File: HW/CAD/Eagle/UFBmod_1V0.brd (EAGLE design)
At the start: 99.7 x 100 mm, 27 parts, among them Q0921 ABS07-32.768KHZ, U0611 MR44V064BMAZAATL, U0911 BNO085, U1311 TPS62745DSSR

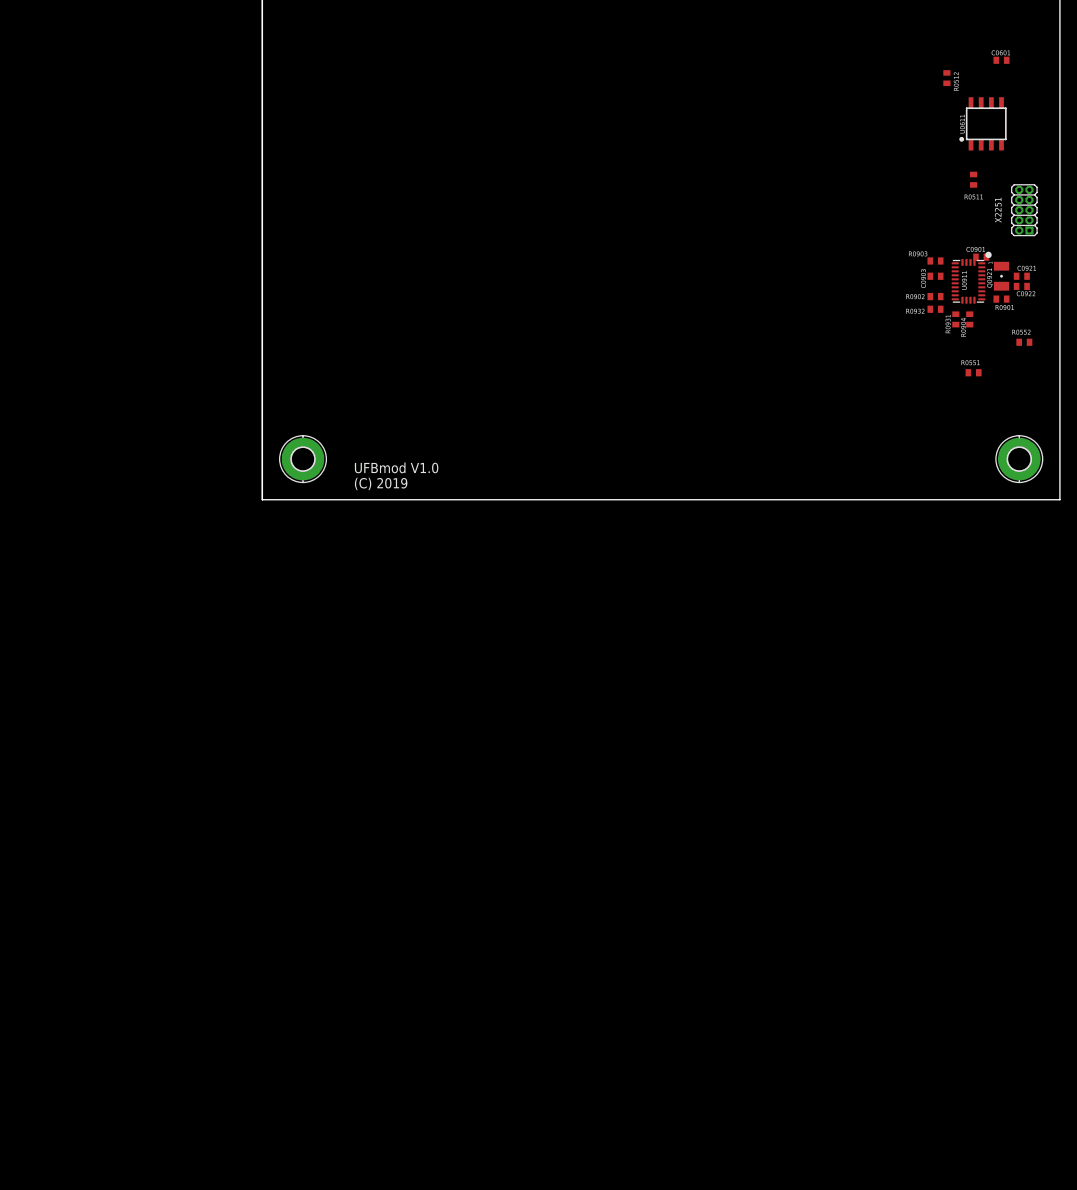
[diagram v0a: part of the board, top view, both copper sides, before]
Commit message: HW_1V0 - CAD/Eagle - Digilent Cmod A7 included, some unwanted sheets removed
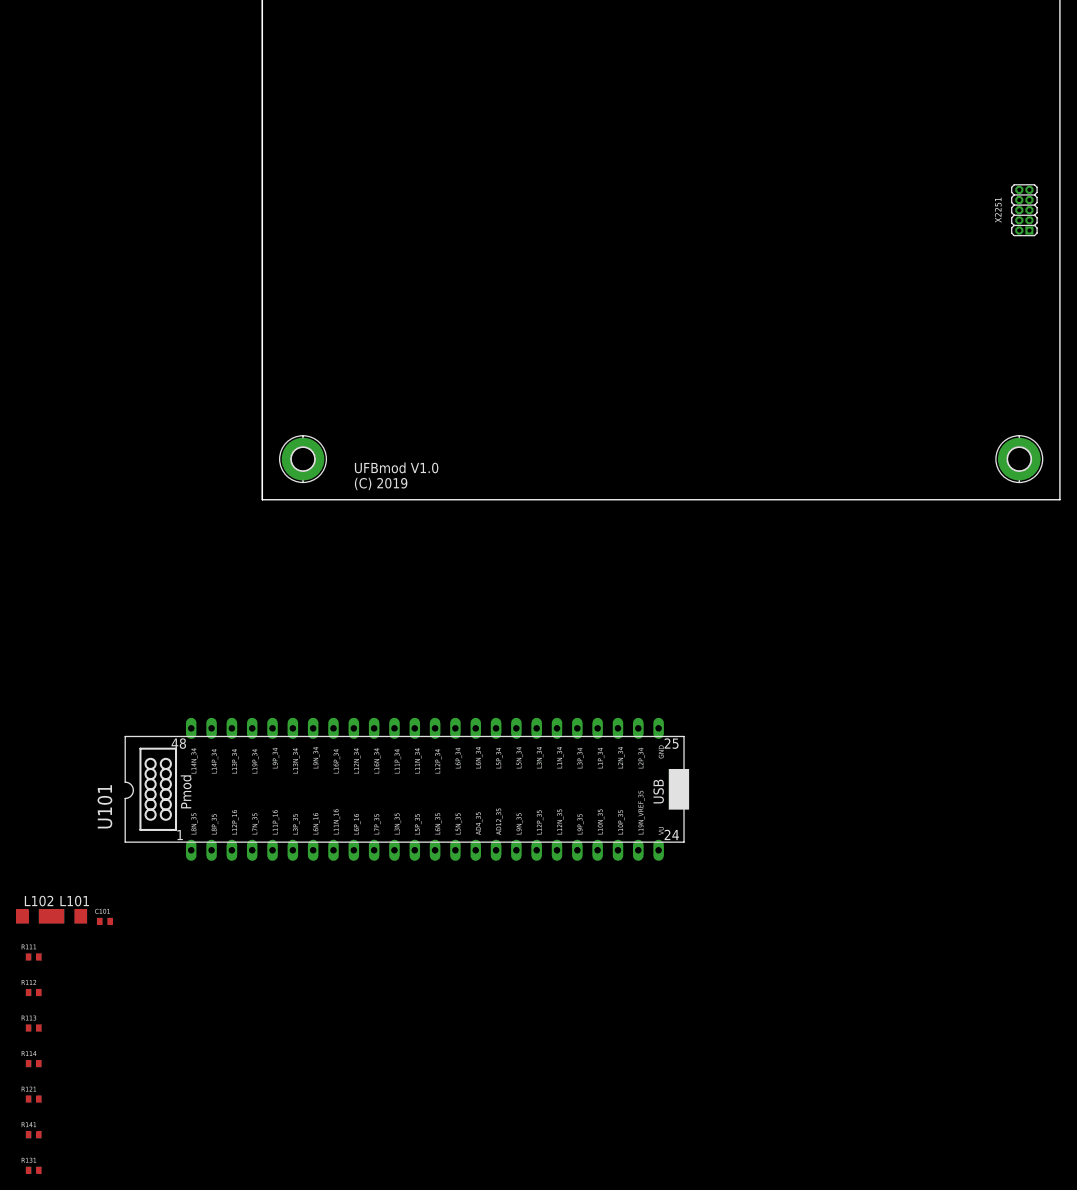
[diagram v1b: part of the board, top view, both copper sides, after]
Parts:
- removed C0601, C0901, C0903: 100nF, df4iah_rcl:C0402
- removed C0921, C0922: 22pF, df4iah_rcl:C0402
- removed Q0921: ABS07-32.768KHZ, df4iah_crystal:ABS07
- removed R0511, R0512: 1kR, df4iah_rcl:R0402
- removed R0551, R0552: 3R, df4iah_rcl:R0402
- removed R0901, R0902, R0904: 33R, df4iah_rcl:R0402
- removed R0903: 47R, df4iah_rcl:R0402
- removed R0931, R0932: 3.9kR, df4iah_rcl:R0402
- removed U0611: MR44V064BMAZAATL, df4iah_memory:SOIC8_150MIL
- removed U0911: BNO085, df4iah_sensors:BNO085_LGA28
- added C101: 100nF, df4iah_rcl:C0402
- added L101, L102: 300R, df4iah_rcl:R1206
- added R111, R112, R113, R114, R121, R131, R141: 47R, df4iah_rcl:R0402
- added U101: DIGILENT_CMOD_A7, df4iah_fpga:DIGILENT_CMOD_A7__DIP48
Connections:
- removed net BNO_CAP: C0903.1, U0911.9
- removed net BNO_CLKSEL1_XOUT32: C0922.1, Q0921.1, U0911.26
- removed net BNO_ENV_SCL: R0932.1, U0911.15
- removed net BNO_ENV_SDA: R0931.1, U0911.16
- removed net BNO_H_CSN: R0904.2, U0911.18
- removed net BNO_INTN: R0902.2, U0911.14
- removed net BNO_MISO: R0901.2, U0911.20
- removed net BNO_PS0_WAKE: R0903.2, U0911.6
- removed net BNO_XIN32: C0921.1, Q0921.2, U0911.27
- removed net PA10: R0511.1, U0611.5
- removed net PA9: R0512.1, U0611.6
- removed net PC10: R0552.1
- removed net PC12: R0551.1
- removed net SPI3_MOSI: R0551.2
- removed net SPI3_SCK: R0552.2
- new net +5V: L101.1
- new net FPGA_MISO: R114.1, U101.42
- new net FPGA_MOSI: R113.1, U101.43
- new net FPGA_SCLK: R111.1, U101.45
- new net FPGA_SELN: R112.1, U101.44
- new net FPGA_TRX_CLKO: R141.2, U101.21
- new net FPGA_TRX_IRQ: R121.1, U101.40
- new net FPGA_TRX_RESETN: R131.2, U101.20
- new net TRX_CLKO: R141.1
- new net TRX_IRQ: R121.2
- new net TRX_MISO: R114.2
- new net TRX_MOSI: R113.2
- new net TRX_RESETN: R131.1
- new net TRX_RXCLKN: U101.48
- new net TRX_RXCLKP: U101.47
- new net TRX_RXDN09N: U101.37
- new net TRX_RXDN24N: U101.1
- new net TRX_RXDP09P: U101.38
- new net TRX_RXDP24P: U101.2
- new net TRX_SCLK: R111.2
- new net TRX_SELN: R112.2
- new net TRX_TXCLKN: U101.19
- new net TRX_TXCLKP: U101.18
- new net TRX_TXDN: U101.34
- new net TRX_TXDP: U101.35
- new net VCCA: C101.2, L101.2, U101.24
- new net VSSA: C101.1, L102.2, U101.25
- net +3V3: no longer C0601.2, C0901.1, R0511.2, R0512.2, R0931.2, R0932.2, U0611.8, U0911.28, U0911.3, U0911.5
- net GND: now also L102.1; no longer C0601.1, C0901.2, C0903.2, C0921.2, C0922.2, U0611.1, U0611.2, U0611.3, U0611.4, U0611.7, U0911.10, U0911.2, U0911.25

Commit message: HW_1V0 - CAD/Eagle - schematics for the RF area expanded
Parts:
- removed R141: 47R, df4iah_rcl:R0402
- added C311, C312, C406, C407, C408, C511, C551, C552, C553: 100nF, df4iah_rcl:C0402
- added C321, C401: 1uF, df4iah_rcl:C0402
- added C403, C404, C521, C531, C532: 1nF, df4iah_rcl:C0402
- added C411, C412: 10nF, df4iah_rcl:C0402
- added C413: 56pF, df4iah_rcl:C0402
- added L401, L402, L403, L404: 300R, df4iah_rcl:R1206
- added L421: MURATA DXW21HN5011BL, df4iah_balun:DXW21HN5011BL
- added L422: Johanson 2450BL15B050E, df4iah_balun:2450BL15B050
- added L521: ? nH, df4iah_rcl:L1812
- added R211, R212: 3.9kR, df4iah_rcl:R0402
- added R321: 100kR, df4iah_rcl:R0402
- added R413: 100R, df4iah_rcl:R0402
- added U301: MAX5217, df4iah_dac:µMAX8
- added U401: AT86RF215-ZU, df4iah_rf:QFN48_7X7-0P5-PAD
- added U411: ASVTX-13-D-26.000MHZ-I05-T, df4iah_osc:ASVTX-13
- added U511: PE4259, df4iah_rf:SC-70_6-LEAD_2X1MM25_0P65
- added U521: (no value), df4iah_rf:QFN16-3X3-0P5-PAD
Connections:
- net FPGA_TRX_RESETN renamed FPGA_TRX_RSTN
- removed net TRX_RESETN: R131.1
- removed net TRX_RXDN09N: U101.37
- removed net TRX_RXDN24N: U101.1
- removed net TRX_RXDP09P: U101.38
- removed net TRX_RXDP24P: U101.2
- new net 26MHZ_DAC_OUT: R321.1, U301.6
- new net FE09_ANT: L521.2, U521.9
- new net FE09_DET: U521.5
- new net FE09_IND: L521.1, U521.10
- new net FE09_MODE: U101.23, U521.16
- new net FE09_RX: C532.1, U521.14
- new net FE09_TX: C531.1, U521.3
- new net FPGA_FE09_DET: U101.15
- new net FPGA_I2C_SCL: R212.1, U101.26, U301.3
- new net FPGA_I2C_SDA: R211.1, U101.27, U301.4
- new net PE09_RF1: C531.2, U511.1
- new net PE09_RF2: C532.2, U511.3
- new net PE09_RFC: C521.1, U511.5
- new net TRX_AVDD0: C407.2, U401.14
- new net TRX_AVDD1: C408.2, U401.47
- new net TRX_AVSS: C404.2, C407.1, C408.1, L401.2, U401.10, U401.16, U401.19, U401.3, U401.45, U401.48, U401.49, U401.6, U401.7
- new net TRX_DEVDD: C403.1, L403.2, U401.21, U401.29, U401.39
- new net TRX_DVDD: C406.2, U401.37
- new net TRX_DVSS: C403.2, C406.1, L402.2, U401.20, U401.23, U401.24, U401.32, U401.38
- new net TRX_EVDD: C404.1, L404.2, U401.15, U401.46
- new net TRX_FEA09: U401.11, U511.4, U521.2
- new net TRX_FEA24: U401.1
- new net TRX_FEB09: U401.12, U521.1
- new net TRX_FEB24: U401.2
- new net TRX_RF09: C521.2, L421.4
- new net TRX_RF09N: L421.2, U401.9
- new net TRX_RF09P: L421.3, U401.8
- new net TRX_RF24: L422.1
- new net TRX_RF24N: L422.4, U401.5
- new net TRX_RF24P: L422.3, U401.4
- new net TRX_RSTN: R131.1, U401.13
- new net TRX_RXD09N: U101.37, U401.30
- new net TRX_RXD09P: U101.38, U401.31
- new net TRX_RXD24N: U101.1, U401.35
- new net TRX_RXD24P: U101.2, U401.36
- new net TRX_TCXO: C412.2, U401.17
- new net VCTCXO_OUT: C412.1, U411.3
- new net VCTCXO_VC: C321.1, R321.2, U411.1
- net +3V3: now also C311.1, C312.1, C401.1, C411.1, C511.1, C551.1, C552.1, C553.1, L403.1, L404.1, R211.2, R212.2, U301.1, U301.5, U301.7, U411.4, U511.6, U521.13, U521.15, U521.7
- net FPGA_TRX_CLKO: now also C413.1, R413.1; no longer R141.2
- net GND: now also C311.2, C312.2, C321.2, C401.2, C411.2, C413.2, C511.2, C551.2, C552.2, C553.2, L401.1, L402.1, L421.1, L422.2, L422.5, U301.2, U301.8, U401.18, U411.2, U511.2, U521.17, U521.4, U521.8
- net TRX_CLKO: now also R413.2, U401.22; no longer R141.1
- net TRX_IRQ: now also U401.40
- net TRX_MISO: now also U401.44
- net TRX_MOSI: now also U401.43
- net TRX_RXCLKN: now also U401.33
- net TRX_RXCLKP: now also U401.34
- net TRX_SCLK: now also U401.41
- net TRX_SELN: now also U401.42
- net TRX_TXCLKN: now also U401.25
- net TRX_TXCLKP: now also U401.26
- net TRX_TXDN: now also U401.27
- net TRX_TXDP: now also U401.28

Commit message: HW_1V0 - CAD/Eagle - schematics for the RF area expanded again
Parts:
- removed U1311: TPS62745DSSR, df4iah_powersupply:WSON-12
- added C591, C593: 0pF, df4iah_rcl:C0402
- added C711: 1nF, df4iah_rcl:C0402
- added J711: (no value), df4iah_connector:USB-B-MICRO-SMD_MOLEX-105017-0001
- added L592: 0nH, df4iah_rcl:L0603
- added PF711: 1.1A/2.2A, rcl:M1206
- added R711: 330kR, df4iah_rcl:R0402
- added U581: B39871B3440U410, df4iah_rf:B3440_3MM-X-3MM
- added U611: TPS62056DGSR, df4iah_powersupply:S-PDSO-G10
- added X599: ANTENNATINY, _c2h:SMA_UFL_PAD_TINY
- C1321: value 10uF -> 22uF
- L1311: value 4.7uH -> 10uH; device df4iah_rcl:L2520 -> df4iah_rcl:L1812
- L521: device df4iah_rcl:L1812 -> df4iah_rcl:L0603
- renumbered X2251 to X721
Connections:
- removed net VBAT_L: C1301.1, U1311.1, U1311.10, U1311.11, U1311.12, U1311.8, U1311.9
- new net ANT: C593.1, L592.2, X599.ANT1, X599.ANT2, X599.ANT3
- new net ANT_MATCH: C591.1, L592.1, U581.5
- new net USB_SHIELD: C711.2, J711.JSHIELD, J711.JSHIELD@2, J711.JSHIELD@3, J711.JSHIELD@4, J711.JSHIELD@5, J711.JSHIELD@6, R711.2
- new net USB_VBUS: J711.VBUS, PF711.2
- net +3V3: now also U611.5; no longer U1311.5
- net +5V: now also C1301.1, PF711.1, U611.1, U611.8
- net FE09_ANT: now also U581.2
- net GND: now also C591.2, C593.2, C711.1, J711.GND, R711.1, U581.1, U581.3, U581.4, U581.6, U611.10, U611.2, U611.3, U611.4, U611.6, U611.7, X599.GND1, X599.GND2, X599.GND3, X599.GND4; no longer U1311.13, U1311.14, U1311.3, U1311.4, U1311.G1, U1311.G2, U1311.G3
- net PMIC3V3_SW: now also U611.9; no longer U1311.2

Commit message: HW_1V0 - CAD/Eagle - board first placement done
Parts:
- removed C1301: 10uF, df4iah_rcl:C0603
- removed C1321: 22uF, df4iah_rcl:C0603
- removed L1311: 10uH, df4iah_rcl:L1812
- added C601: 10uF, df4iah_rcl:C0603
- added C621: 22uF, df4iah_rcl:C0603
- added L611: 10uH, df4iah_rcl:L1812
- moved PF711 402.3 mm to (49.5, 80.0), turned to 90 degrees
- moved R711 399.7 mm to (38.1, 85.1), turned to 90 degrees
- moved C711 399.1 mm to (39.4, 85.1), turned to 90 degrees
- moved J711 377.7 mm to (45.7, 88.9), turned to 180 degrees
- moved U611 352.3 mm to (34.3, 80.0), flipped to the bottom, turned to 90 degrees
- moved X599 346.0 mm to (19.1, 89.5), turned to 90 degrees
- moved U581 339.0 mm to (17.8, 71.1)
- moved C591 327.3 mm to (17.8, 77.5), turned to 180 degrees
- moved L592 325.8 mm to (19.1, 80.0), turned to 90 degrees
- moved C593 323.6 mm to (17.8, 82.5), turned to 180 degrees
- moved C551 298.6 mm to (14.0, 62.2), turned to 180 degrees
- moved C552 296.8 mm to (14.0, 64.8), turned to 180 degrees
- moved C553 294.4 mm to (21.6, 64.8)
- moved L521 287.7 mm to (17.8, 67.3)
- moved U521 282.5 mm to (17.8, 63.5), turned to 90 degrees
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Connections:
- net +3V3: now also C621.1, L611.1; no longer C1321.1, L1311.1
- net +5V: now also C601.1; no longer C1301.1
- net GND: now also C601.2, C621.2; no longer C1301.2, C1321.2
- net PMIC3V3_SW: now also L611.2; no longer L1311.2
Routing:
- net USB_SHIELD: track 0.00 -> 17.9 mm
- net GND: track 0.00 -> 8.33 mm
- net VCCA: track 0.00 -> 7.90 mm
- net VSSA: track 0.00 -> 7.90 mm
- net USB_VBUS: track 0.00 -> 4.97 mm
- net FPGA_TRX_RSTN: track 0.00 -> 4.43 mm
- net FPGA_SELN: track 0.00 -> 4.43 mm
- net FPGA_SCLK: track 0.00 -> 4.43 mm
- net FPGA_MOSI: track 0.00 -> 4.43 mm
- net +5V: track 0.00 -> 2.26 mm, vias 0 -> 1
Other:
- board size 99.7 x 100 mm -> 78.1 x 89.8 mm
- board text added: "UFBmod V1.0 (C) 2019 by DF4IAH"
- board text removed: "LoRaWAN: -WiFi für das Internet der Dinge-"
- board text removed: "Reed"
- board text removed: "UFBmod V1.0 (C) 2019"
- board text removed: "contact"
- board text removed: "www.IoT4Bees.de"

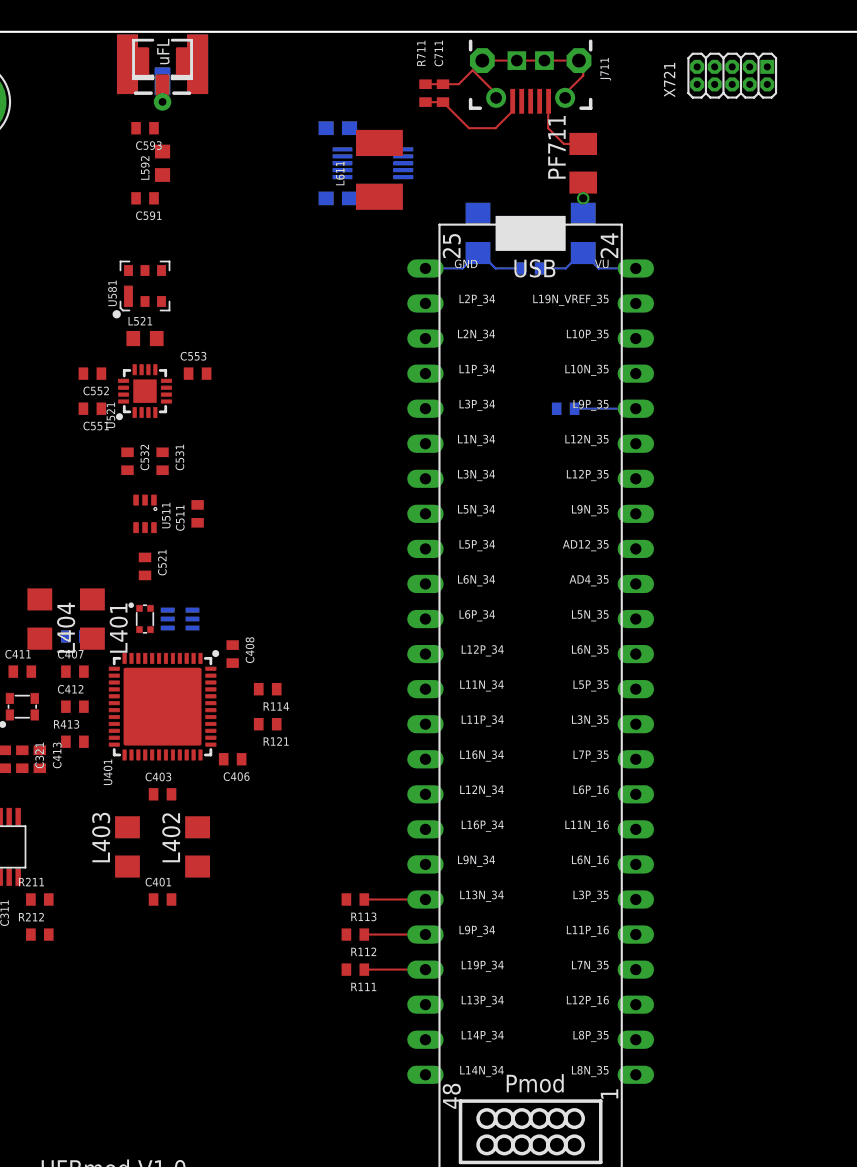
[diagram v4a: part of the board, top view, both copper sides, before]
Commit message: HW_1V0 - CAD/Eagle - routing started, Due to 100R-impedance lines 4layers needed.
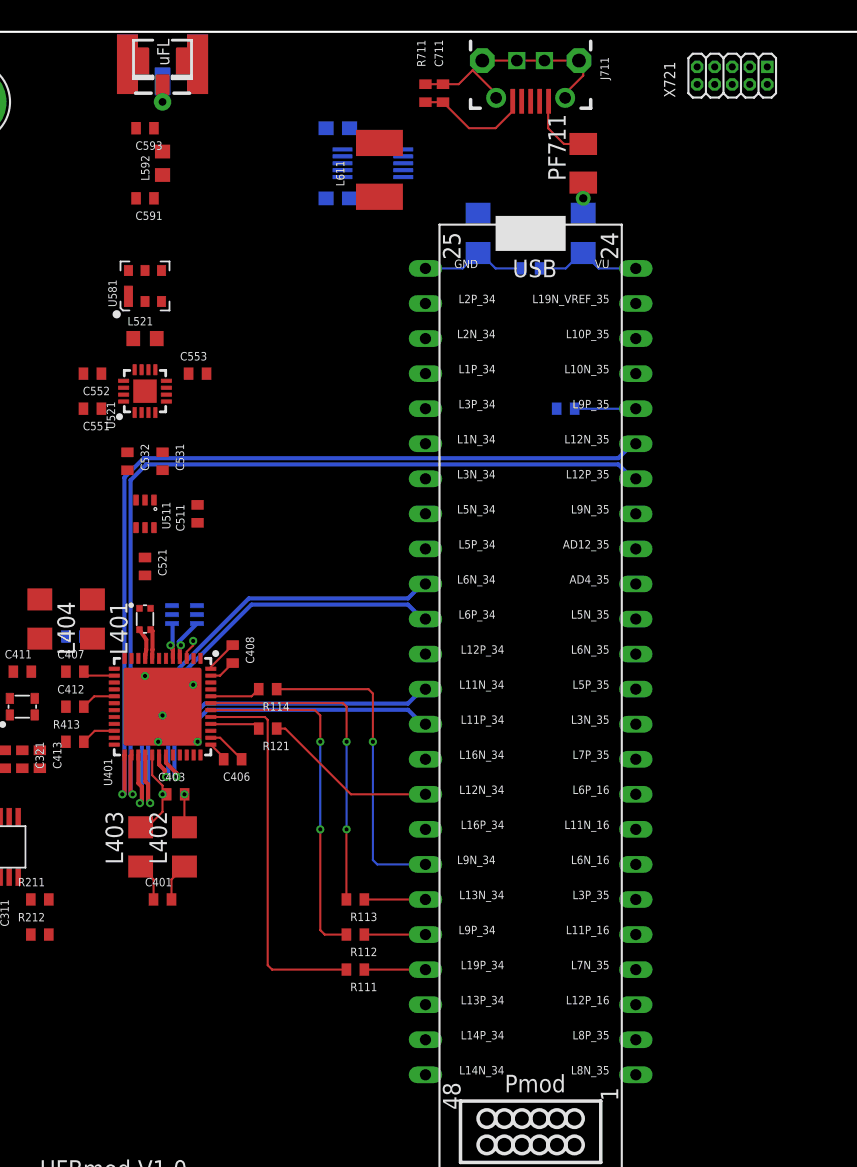
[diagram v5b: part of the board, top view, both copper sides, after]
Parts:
- moved C403 0.95 mm to (20.0, 34.3)
- moved L402 0.95 mm to (20.6, 30.5)
- moved L403 0.95 mm to (17.5, 30.5)
- moved L422 0.45 mm to (20.6, 47.3)
- moved R121 0.32 mm to (26.7, 39.1)
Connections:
- net TRX_RF09N renamed TRX_RF09_N
- net TRX_RF09P renamed TRX_RF09_P
- net TRX_RF24N renamed TRX_RF24_N
- net TRX_RF24P renamed TRX_RF24_P
- net TRX_RXCLKN renamed TRX_RXCLK_N
- net TRX_RXCLKP renamed TRX_RXCLK_P
- net TRX_RXD09N renamed TRX_RXD09_N
- net TRX_RXD09P renamed TRX_RXD09_P
- net TRX_RXD24N renamed TRX_RXD24_N
- net TRX_RXD24P renamed TRX_RXD24_P
- net TRX_TXCLKN renamed TRX_TXCLK_N
- net TRX_TXCLKP renamed TRX_TXCLK_P
- net TRX_TXDN renamed TRX_TXD_N
- net TRX_TXDP renamed TRX_TXD_P
- net GND: no longer U401.18
- net TRX_AVSS: now also U401.18
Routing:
- net TRX_TXCLK_N: track 0.00 -> 64.2 mm, vias 0 -> 1
- net TRX_TXCLK_P: track 0.00 -> 63.5 mm, vias 0 -> 1
- net TRX_TXD_N: track 0.00 -> 35.2 mm, vias 0 -> 1
- net TRX_TXD_P: track 0.00 -> 34.4 mm, vias 0 -> 1
- net TRX_SCLK: track 0.00 -> 27.8 mm
- net TRX_SELN: track 0.00 -> 25.7 mm, vias 0 -> 2
- net TRX_RXD09_N: track 0.00 -> 24.9 mm, vias 0 -> 1
- net TRX_RXD09_P: track 0.00 -> 24.3 mm, vias 0 -> 1
- net TRX_MOSI: track 0.00 -> 23.9 mm, vias 0 -> 2
- net FPGA_MISO: track 0.00 -> 23.1 mm, vias 0 -> 1
- net TRX_AVSS: track 0.00 -> 15.9 mm, vias 0 -> 6
- net FPGA_TRX_IRQ: track 0.00 -> 12.8 mm
- net TRX_DEVDD: track 0.00 -> 6.78 mm, vias 0 -> 1
- net TRX_DVSS: track 0.00 -> 5.28 mm, vias 0 -> 1
- net TRX_MISO: track 0.00 -> 3.69 mm
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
